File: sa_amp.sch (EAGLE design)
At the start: 87 parts, among them U4 TPA3255

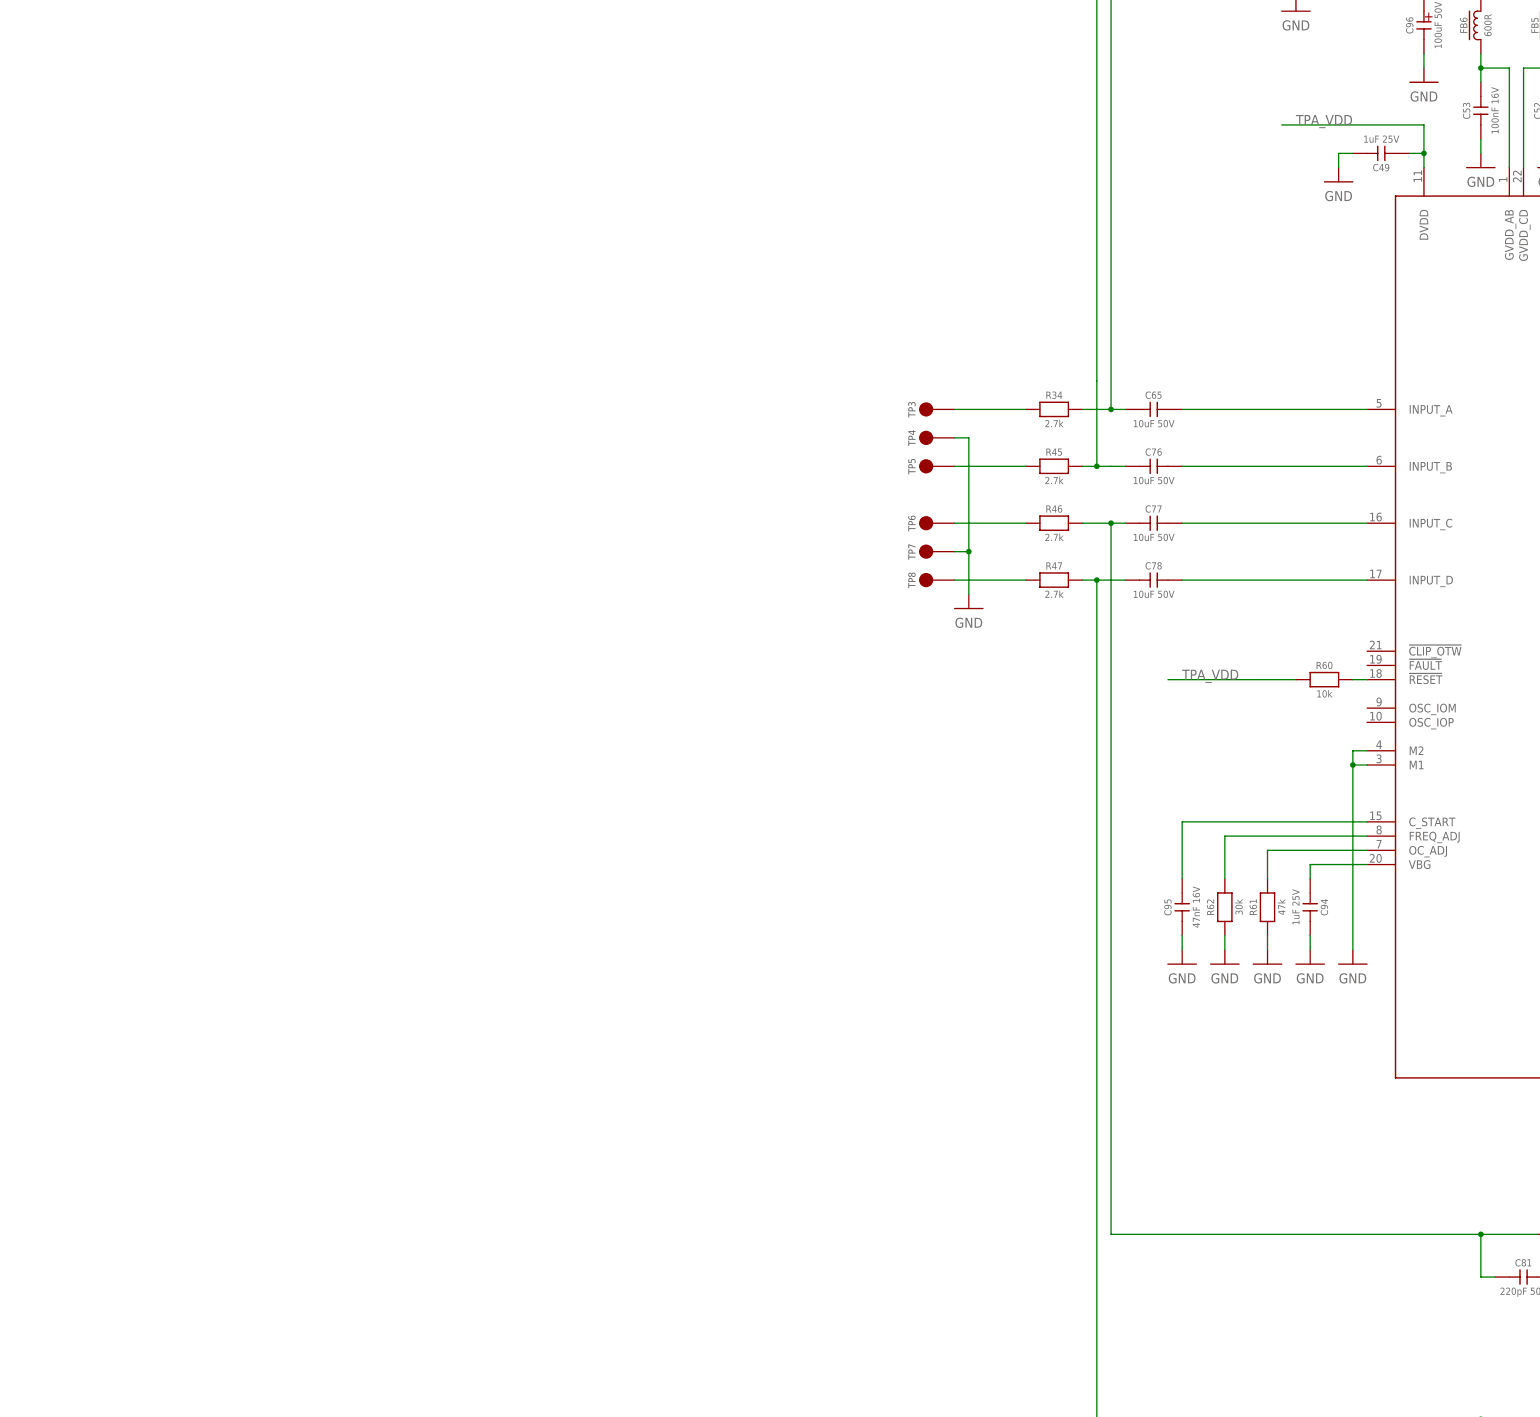
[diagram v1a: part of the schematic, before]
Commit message: Master reset circuitry added
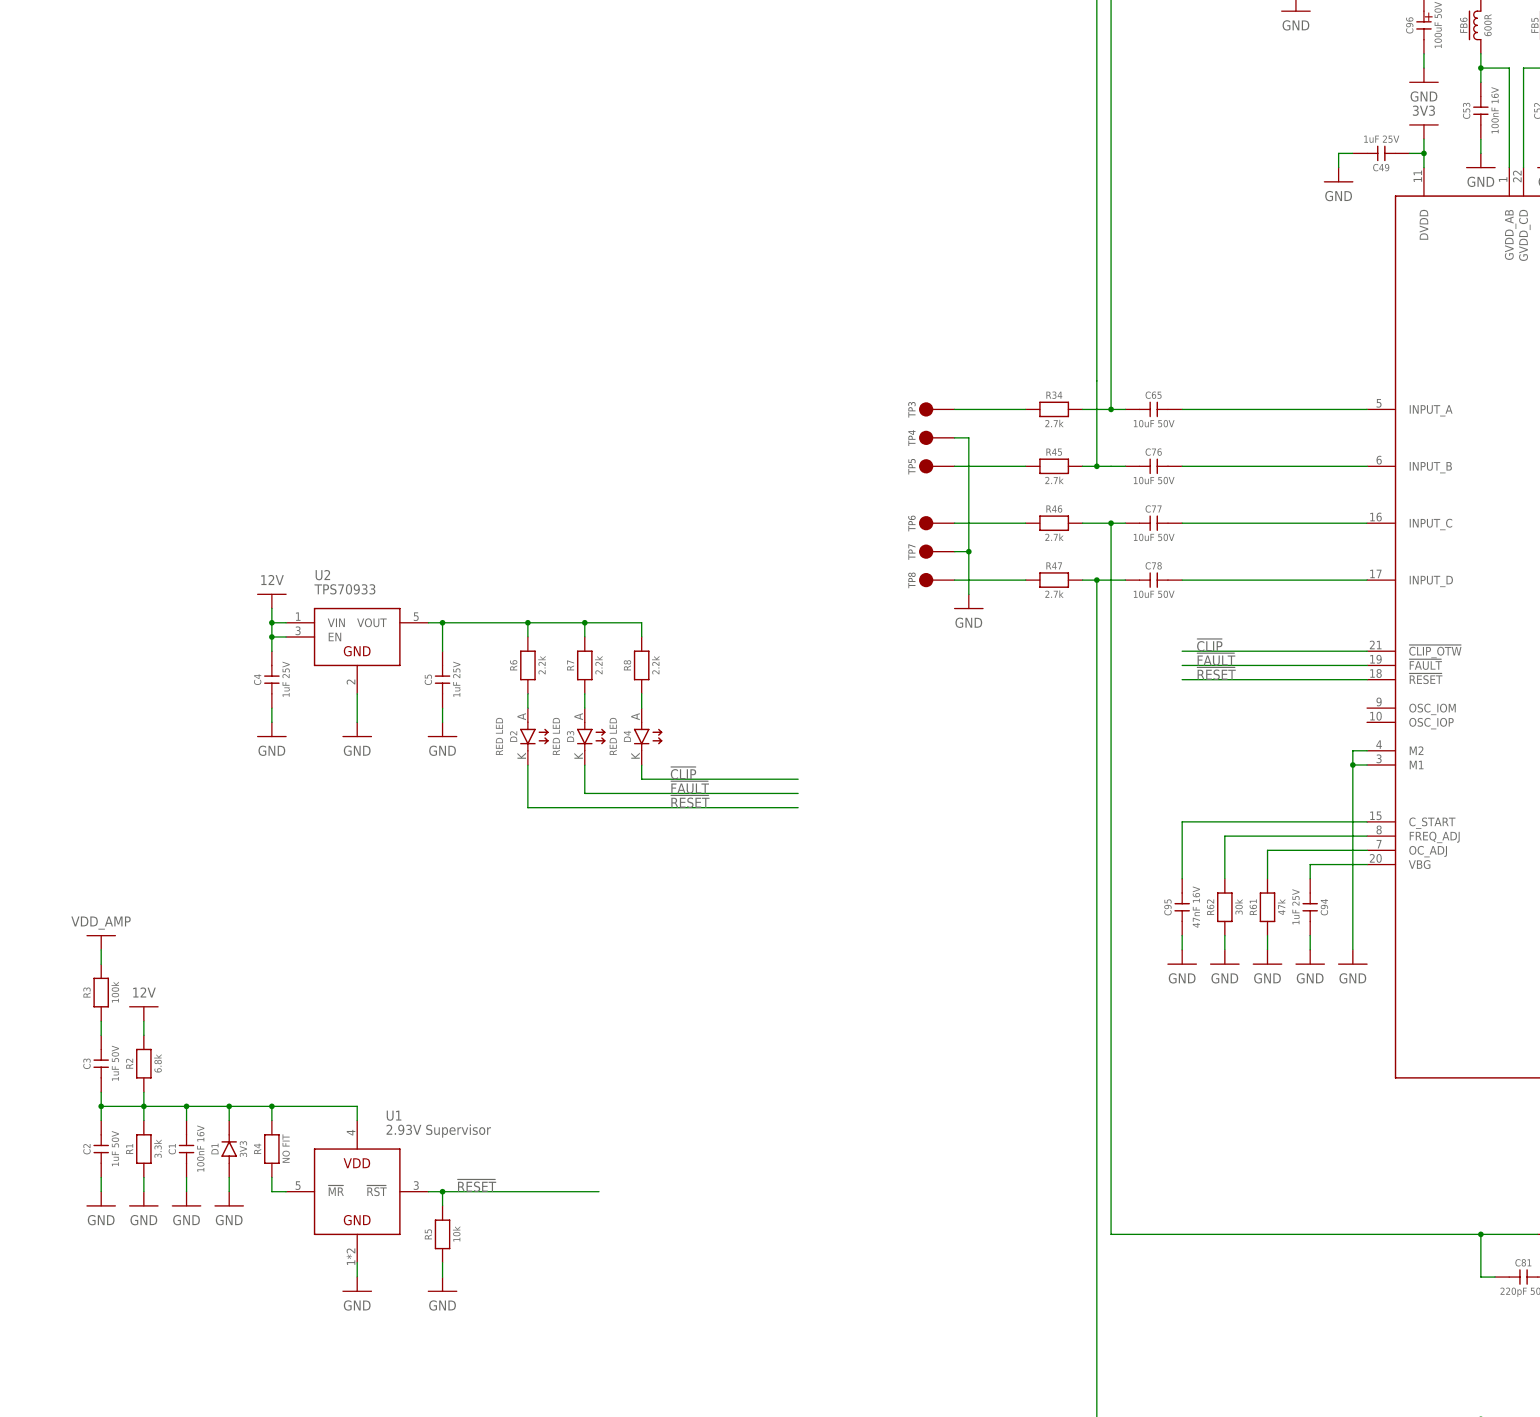
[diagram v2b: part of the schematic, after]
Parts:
- removed R60: 10k, r_0603:ERJ3EKF1002V
- added C1: 100nF 16V, CAPACITORS:CL10B104KO8WPNC
- added C2, C3: 1uF 50V, CAPACITORS:CL31B105KBHNNNE
- added C4, C5: 1uF 25V, CAPACITORS:CL10A105KA8NNNC
- added D1: 3V3, DIODES:MM3Z3V3ST1G
- added D2, D3, D4: RED LED, OPTO:150060RS75000
- added R1: 3.3k, r_0603:ERJ3EKF3301V
- added R2: 6.8k, r_0603:ERJ3EKF6801V
- added R3: 100k, r_0603:ERJ3EKF1003V
- added R4: NO FIT, r_0603:ERJ3EKF1003V
- added R5: 10k, r_0603:ERJ3EKF1002V
- added R6, R7, R8: 2.2k, r_0603:ERJ3EKF2201V
- added U1: 2.93V Supervisor, ICs:TPS3802K33DCK
- added U2: TPS70933, ICs:TPS70933DBVT
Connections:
- removed net N$90: R60.2, U4.!RESET
- removed net TPA_VDD: C49.1, R60.1, U4.DVDD
- new net !CLIP: D4.K, U4.!CLIP_OTW
- new net !FAULT: D3.K, U4.!FAULT
- new net !RESET: D2.K, R5.2, U1.!RST, U4.!RESET
- new net 3V3: C49.1, U4.DVDD
- new net N$10: D2.A, R6.1
- new net N$11: D3.A, R7.1
- new net N$12: D4.A, R8.1
- new net N$13: C5.2, R6.2, R7.2, R8.2, U2.VOUT
- new net N$7: R4.1, U1.!MR
- new net N$8: C1.2, C2.2, C3.1, D1.K, R1.2, R2.1, R4.2, U1.VDD
- new net N$9: C3.2, R3.1
- net 12V: now also C4.2, R2.2, U2.EN, U2.VIN
- net GND: now also C1.1, C2.1, C4.1, C5.1, D1.A, R1.1, R5.1, U1.GND, U2.GND
- net VDD_AMP: now also R3.2

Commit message: New concept TPA3255 amplifier
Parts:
- removed C57: 4700uF 63V, CAPACITORS:B41231C8478M000
- removed C66, C67, C79, C80, C81, C82, C83, C84: 220pF 50V, CAPACITORS:CC0603JRNPO9BN221
- removed D4: RED LED, OPTO:150060RS75000
- removed R34, R45, R46, R47: 2.7k, r_0603:ERJ3EKF2701V
- removed R35, R48, R50, R52: 33k, r_0603:ERJ3EKF3302V
- removed R36, R49, R51, R53: 10k, r_0603:ERJ3EKF1002V
- removed TP1, TP2, TP3, TP4, TP5, TP6, TP7, TP8: 2MM_TEST_POINT, MISC:2MM_TEST_POINT
- added C6, C7, C9: 100nF 100V, CAPACITORS:06031C104KAT2A
- added C8: 1uF 25V, CAPACITORS:CL10A105KA8NNNC
- added CN1, CN2, CN3, CN4, CN5, CN6: PCB Tab, CONNECTORs:PCB_TAB_SMALL
- added CN7: TC2030, tag-connect:TC2030-MCP
- added CN8: NO FIT, CONNECTORs:1X3_HEADER
- added HOLE5, HOLE6: PCB Tab, CONNECTORs:PCB_TAB
- added MECH5, MECH6: 6mm x 3mm, MISC:MOUNTHOLE
- added Q1: 2N7002, TRANSISTORs:2N7002P,215
- added RL1, RL2: RT424012, ELECTROMECH:RT424012
- added U3: LM7812, ICs:7812CTG
- added U5: LM317, ICs:LM317LCPK
- C1: value 100nF 16V -> 0.1uF 16V; device CAPACITORS:CL10B104KO8WPNC -> c_0603:0603YC104K4T4A
- C2: value 1uF 50V -> 0.1uF 16V; device CAPACITORS:CL31B105KBHNNNE -> c_0603:0603YC104K4T4A
- C3: value 1uF 50V -> 100nF 100V; device CAPACITORS:CL31B105KBHNNNE -> CAPACITORS:06031C104KAT2A
- C4: value 1uF 25V -> 100uF 50V; device CAPACITORS:CL10A105KA8NNNC -> CAPACITORS:107CKR050M
- C5: value 1uF 25V -> 100nF 100V; device CAPACITORS:CL10A105KA8NNNC -> CAPACITORS:06031C104KAT2A
- D1: value 3V3 -> PMEG4010BEA; device DIODES:MM3Z3V3ST1G -> DIODES:PMEG4010BEA
- D2, D3: value RED LED -> PESD5Z3.3; device OPTO:150060RS75000 -> DIODES:PESD5Z3.3
- HOLE1, HOLE2, HOLE3, HOLE4: value MOUNTHOLE_METAL6X3 -> PCB Tab; device MISC:MOUNTHOLE_METAL6X3 -> CONNECTORs:PCB_TAB
- R1: value 3.3k -> 47k; device r_0603:ERJ3EKF3301V -> r_0603:ERJ3EKF4702V
- R2: value 6.8k -> 47k; device r_0603:ERJ3EKF6801V -> r_0603:ERJ3EKF4702V
- R3: value 100k -> 240R; device r_0603:ERJ3EKF1003V -> r_0603:CRCW0603240RFKEA
- R4: value NO FIT -> 390R; device r_0603:ERJ3EKF1003V -> r_0603:CRCW0603390RFKEA
- R5: value 10k -> 1k; device r_0603:ERJ3EKF1002V -> r_0603:CRCW06031K00FKEB
- R6: value 2.2k -> 18k; device r_0603:ERJ3EKF2201V -> r_0603:CRCW060318K0FKEA
- R7: value 2.2k -> 10k; device r_0603:ERJ3EKF2201V -> r_0603:CRCW060310K0FKTA
- R8: value 2.2k -> 36k; device r_0603:ERJ3EKF2201V -> r_0603:CRCW060336K0FKEA
- U1: value 2.93V Supervisor -> STM32L031G6; device ICs:TPS3802K33DCK -> ICs:STM32L031G6
- U2: value TPS70933 -> 15V REG; device ICs:TPS70933DBVT -> ICs:SRH05S15
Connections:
- removed net !CLIP: D4.K, U4.!CLIP_OTW
- removed net !FAULT: D3.K, U4.!FAULT
- removed net !RESET: D2.K, R5.2, U1.!RST, U4.!RESET
- removed net N$10: D2.A, R6.1
- removed net N$11: D3.A, R7.1
- removed net N$12: D4.A, R8.1
- removed net N$64: C66.2, C67.1, R36.1
- removed net N$7: R4.1, U1.!MR
- removed net N$78: C76.1, C79.1, R45.2, R48.1
- removed net N$80: C79.2, C80.1, R49.1
- removed net N$81: C78.1, C83.1, R47.2, R52.1
- removed net N$83: C81.2, C82.1, R51.1
- removed net N$85: C84.2, C91.2, C92.2, C93.2, HOLE4.1, L8.2, R52.2
- removed net N$86: C83.2, C84.1, R53.1
- new net 15V: C4.K, C5.1, D1.K, RL1A.A1, RL2A.A1, U2.VOUT, U3.VIN
- new net N$14: C49.1, U4.DVDD
- new net N$16: C78.1, CN6.1
- new net N$17: C76.1, CN3.1
- new net N$18: C77.1, CN4.1
- new net PROC_!RESET: CN7.!RESET, U1.NRST
- new net PROC_SWCLK: CN7.SWCLK, U1.PA14
- new net PROC_SWDIO: CN7.SWDIO, U1.PA13
- new net PROC_UART_RX: CN8.2, U1.PA3
- new net PROC_UART_TX: CN8.1, U1.PA2
- new net PSU_12V_SENSE: C9.1, D3.K, R7.2, R8.2, U1.PA1
- new net PSU_VDD_AMP_SENSE: C3.1, D2.K, R5.2, R6.2, U1.PA0
- new net RLY_EN: Q1.G, R1.2, U1.PB3
- new net TPA_!CLIP: U1.PC15, U4.!CLIP_OTW
- new net TPA_!FAULT: U1.PC14, U4.!FAULT
- new net TPA_!RESET: U1.PA15, U4.!RESET
- net 12V: now also C6.1, C7.1, R8.1, U3.VOUT, U5.VIN; no longer C4.2, R2.2, TP1.P$1, U2.EN, U2.VIN
- net 3V3: now also C1.2, C2.2, C8.2, CN7.VCC, R3.2, U1.VDD, U1.VDDA, U5.VOUT; no longer C49.1, U4.DVDD
- net GND: now also C3.2, C4.A, C5.2, C6.2, C7.2, C8.1, C9.2, CN2.1, CN5.1, CN7.GND, CN8.3, D2.A, D3.A, HOLE6.1, Q1.S, R2.1, R4.1, R7.1, U1.VSS, U3.GND; no longer C4.1, C5.1, C57.K, D1.A, R36.2, R49.2, R51.2, R53.2, TP2.P$1, TP4.P$1, TP7.P$1, U1.GND
- net N$13: now also R3.1, R4.2, U5.ADJ; no longer C5.2, R6.2, R7.2, R8.2, U2.VOUT
- net N$2: now also C91.2, C92.2, C93.2, L8.2, RL2C.3; no longer C77.1, C81.1, R46.2, R50.1
- net N$3: now also HOLE4.1, RL2C.1; no longer R34.1, TP3.P$1
- net N$4: now also HOLE1.1, RL1B.1; no longer R45.1, TP5.P$1
- net N$5: now also HOLE2.1, RL1C.1; no longer R46.1, TP6.P$1
- net N$6: now also HOLE3.1, RL2B.1; no longer R47.1, TP8.P$1
- net N$62: now also CN1.1; no longer C66.1, R34.2, R35.1
- net N$63: now also RL1B.3; no longer C67.2, HOLE1.1, R35.2
- net N$79: now also RL1C.3; no longer C80.2, HOLE2.1, R48.2
- net N$8: now also R2.2, U1.BOOT0; no longer C1.2, C2.2, C3.1, D1.K, R1.2, R2.1, R4.2, U1.VDD
- net N$82: now also RL2B.3; no longer C82.2, HOLE3.1, R50.2
- net N$9: now also D1.A, Q1.D, RL1A.A2, RL2A.A2; no longer C3.2, R3.1
- net VDD_AMP: now also HOLE5.1, R6.1, U2.VIN; no longer C57.A, R3.2
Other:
- moved on the sheet: C1, C2, C3, C5, D1, R1, R2, R3, R4, R5, R6, R7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

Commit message: amp fixed
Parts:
- removed R33, R55, R57, R59: 2R0, RESISTORS:CRCW12062R00FNEA
- C63, C86, C89, C92: value 10nF 250V -> 1nF 50V; device CAPACITORS:885342206006 -> CAPACITORS:CL10B102KB8NNNC
- C64, C87, C90, C93: value 220nF 100V -> 10nF 250V; device CAPACITORS:C3216X7R2A224K115AA -> CAPACITORS:885342206006
- R32, R54, R56, R58: value 2R0 -> 3R3; device RESISTORS:CRCW12062R00FNEA -> RESISTORS:RL73H3AR10FTDF
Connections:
- net 15V: now also C4.A; no longer C4.K
- net GND: now also C4.K; no longer C4.A, R33.1, R55.1, R57.1, R59.1
- net N$60: no longer R33.2
- net N$87: no longer R55.2
- net N$88: no longer R57.2
- net N$89: no longer R59.2
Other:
- note added: "UNCONTROLLED WHEN PRINTED"
- moved on the sheet: C1, C2, C3, C4, C49, C5, C50, C51, C52, C53, C54, C55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
